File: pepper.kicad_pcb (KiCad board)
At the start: 2 copper layers, 73 x 37 mm, 48 parts, among them J1 USB, J2 Debug, Q1 BSS138, SW1 Reset, SW2 Boot, SW3 Action, U1 ESP32-S3-WROOM-1, U2 AP2112K-3.3

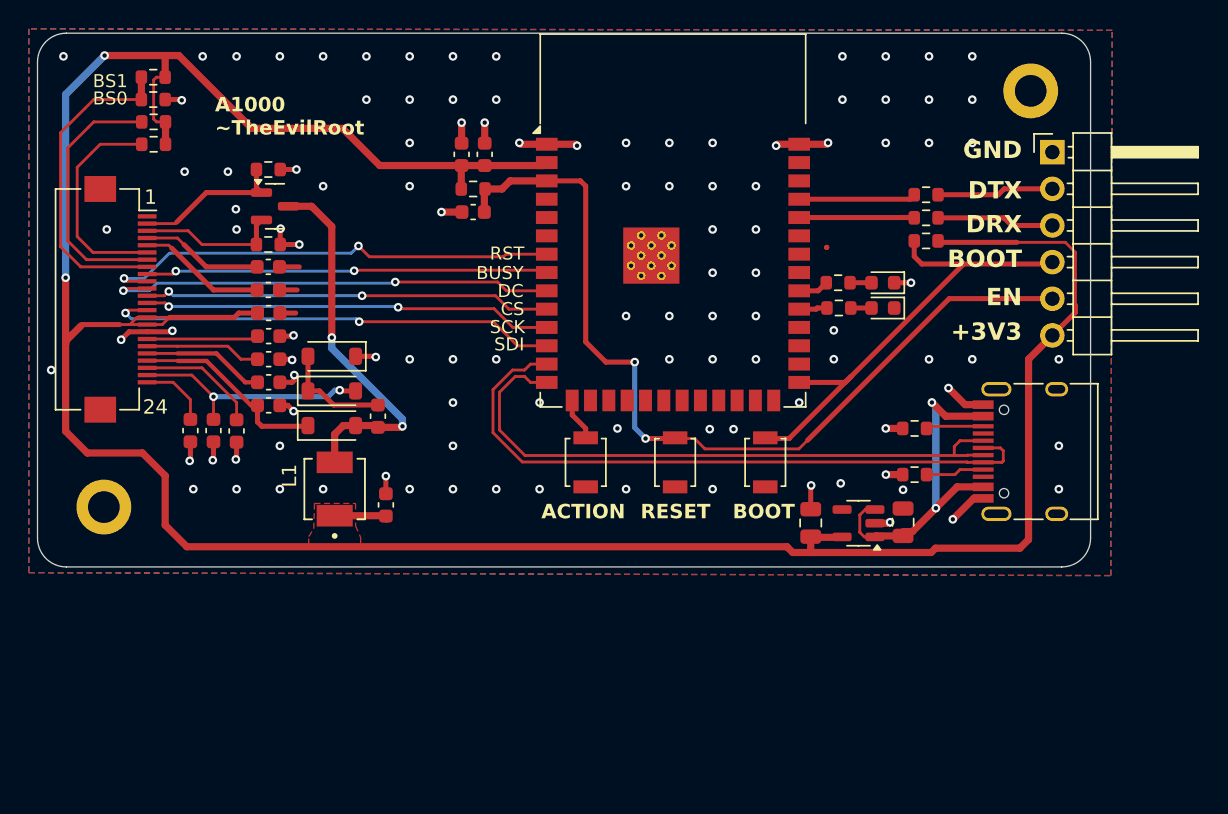
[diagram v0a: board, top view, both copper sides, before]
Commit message: Redesign. Bottom control panel
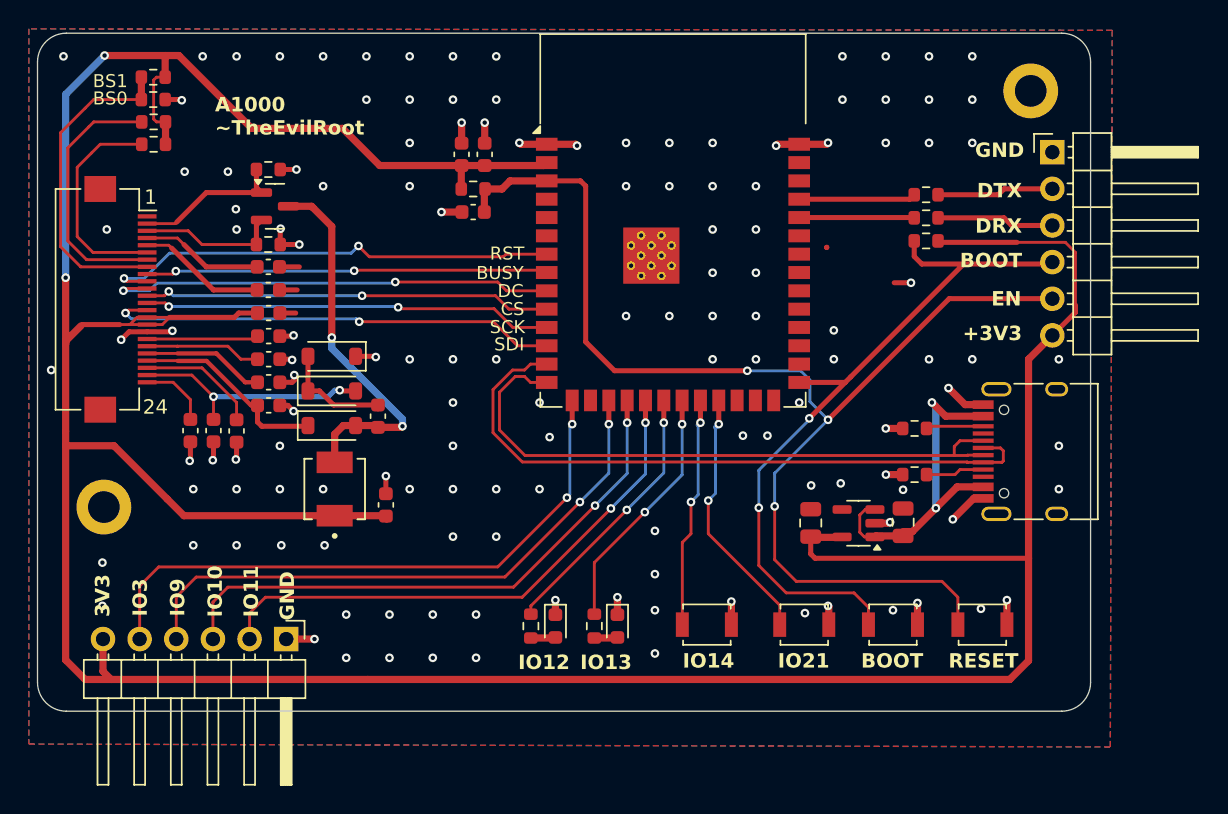
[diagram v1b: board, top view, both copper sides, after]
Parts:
- added J3: Conn_01x06, Connector_PinHeader_2.54mm:PinHeader_1x06_P2.54mm_Horizontal, F.Cu at (151.0, 118.4)
- added SW4: Action, Button_Switch_SMD:SW_SPST_B3U-1000P, F.Cu at (180.2, 117.4)
- moved D4 32.9 mm to (169.7, 117.5), turned to -90 degrees
- moved R9 31.9 mm to (168.0, 117.5), turned to 90 degrees
- moved D5 28.7 mm to (174.0, 117.5), turned to -90 degrees
- moved R10 27.8 mm to (172.4, 117.5), turned to 90 degrees
- moved SW1 24.1 mm to (199.3, 117.4), turned to 180 degrees
- moved SW3 18.9 mm to (186.9, 117.4), turned to 180 degrees
- moved SW2 14.3 mm to (193.1, 117.4), turned to 180 degrees
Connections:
- net /ESP_IO38A renamed /ESP_LED2A
- net /ESP_IO39A renamed /ESP_LED1A
- R10 pad 2: /ESP_IO38 -> /ESP_IO13
- R9 pad 2: /ESP_IO39 -> /ESP_IO12
- SW3 pad 2: /ESP_IO3 -> /ESP_IO21
- U1 pad 17: unconnected-(U1-IO9-Pad17) -> /ESP_IO9
- U1 pad 18: unconnected-(U1-IO10-Pad18) -> /ESP_IO10
- U1 pad 19: unconnected-(U1-IO11-Pad19) -> /ESP_IO11
- U1 pad 20: unconnected-(U1-IO12-Pad20) -> /ESP_IO12
- U1 pad 21: unconnected-(U1-IO13-Pad21) -> /ESP_IO13
- U1 pad 22: unconnected-(U1-IO14-Pad22) -> /ESP_IO14
- U1 pad 23: unconnected-(U1-IO21-Pad23) -> /ESP_IO21
- U1 pad 31: /ESP_IO38 -> unconnected-(U1-IO38-Pad31)
- U1 pad 32: /ESP_IO39 -> unconnected-(U1-IO39-Pad32)
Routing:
- net +3V3: track 198.9 -> 257.3 mm
- net /ESP_IO9: track 0.00 -> 41.5 mm, vias 0 -> 2
- net /ESP_IO10: track 0.00 -> 40.0 mm, vias 0 -> 2
- net /ESP_IO3: track 3.03 -> 42.7 mm, vias 0 -> 2
- net /ESP_IO11: track 0.00 -> 38.3 mm, vias 0 -> 2
- net /ESP_EN: track 62.2 -> 85.6 mm, vias 2 -> 3
- net /ESP_IO12: track 0.00 -> 18.6 mm, vias 0 -> 2
- net /ESP_IO21: track 0.00 -> 17.9 mm, vias 0 -> 2
- net /ESP_BOOT: track 33.5 -> 51.0 mm, vias 0 -> 2
- net /ESP_IO13: track 0.00 -> 17.3 mm, vias 0 -> 2
- net /ESP_IO14: track 0.00 -> 16.1 mm, vias 0 -> 2
- net GND: track 46.7 -> 55.7 mm, vias 110 -> 137
- net /ESP_IO39: track 2.11 -> 0.00 mm
- net /ESP_IO38: track 1.96 -> 0.00 mm
- removed copper zone on F.Cu, net +3V3
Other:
- board size 73 x 37 mm -> 73 x 47 mm
- board text added: "3V3"
- board text added: "IO10"
- board text added: "IO11"
- board text added: "IO12"
- board text added: "IO13"
- board text added: "IO14"
- board text added: "IO21"
- board text added: "IO3"
- board text added: "IO9"
- board text removed: "ACTION"

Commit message: Simple order 1
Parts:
- added SW5: Action, Button_Switch_SMD:SW_SPST_TL3342, F.Cu at (185.3, 117.2)
- added SW6: Action, Button_Switch_SMD:SW_SPST_TL3342, F.Cu at (195.9, 117.2)
- SW3, SW4: footprint Button_Switch_SMD:SW_SPST_B3U-1000P -> Button_Switch_SMD:SW_SPST_TL3342
- moved SW1 38.1 mm to (192.0, 80.0), turned to 90 degrees
- moved SW2 37.6 mm to (197.0, 80.0), turned to 90 degrees
- moved D5 18.5 mm to (155.7, 120.3), turned to 180 degrees
- moved R10 16.7 mm to (155.7, 118.7), turned to 0 degrees
- moved SW4 15.9 mm to (164.3, 117.5)
- moved D4 14.0 mm to (155.7, 116.7), turned to 180 degrees
- moved R9 12.5 mm to (155.7, 115.0), turned to 0 degrees
- moved SW3 11.4 mm to (175.6, 117.2)
- moved J1 1.05 mm to (204.4, 105.4)
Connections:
- U1 pad 24: unconnected-(U1-IO47-Pad24) -> /ESP_IO47
- U1 pad 25: unconnected-(U1-IO48-Pad25) -> /ESP_IO48
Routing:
- net /ESP_IO48: track 0.00 -> 27.2 mm
- net /ESP_IO47: track 0.00 -> 23.9 mm
- net /ESP_IO13: track 17.3 -> 32.0 mm, vias 2 -> 0
- net /ESP_EN: track 85.6 -> 99.5 mm, vias 3 -> 2
- net GND: track 55.7 -> 67.3 mm, vias 137 -> 95
- net /ESP_IO14: track 16.1 -> 26.1 mm, vias 2 -> 0
- net /ESP_IO12: track 18.6 -> 28.3 mm, vias 2 -> 0
- net /ESP_IO21: track 17.9 -> 23.3 mm, vias 2 -> 0
- net /ESP_BOOT: track 51.0 -> 47.9 mm, vias 2 -> 0
- net +5V: track 23.8 -> 20.7 mm
- net /USB_D+: track 43.6 -> 46.1 mm, vias 0 -> 2
- net /USB_D-: track 45.9 -> 47.6 mm, vias 0 -> 2
- net +3V3: track 257.3 -> 258.4 mm, vias 2 -> 1
- net /USB_CC2: track 3.99 -> 5.04 mm
- net /USB_CC1: track 4.07 -> 5.12 mm
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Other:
- board text added: "pepper A2113 ~TheEvilRoot"
- board text removed: "A1000 ~TheEvilRoot"
- board text removed: "IO12"
- board text removed: "IO13"
- board text removed: "IO14"
- board text removed: "IO21"
